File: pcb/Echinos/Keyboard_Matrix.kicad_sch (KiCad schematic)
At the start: 62 parts, among them J5 Joystick

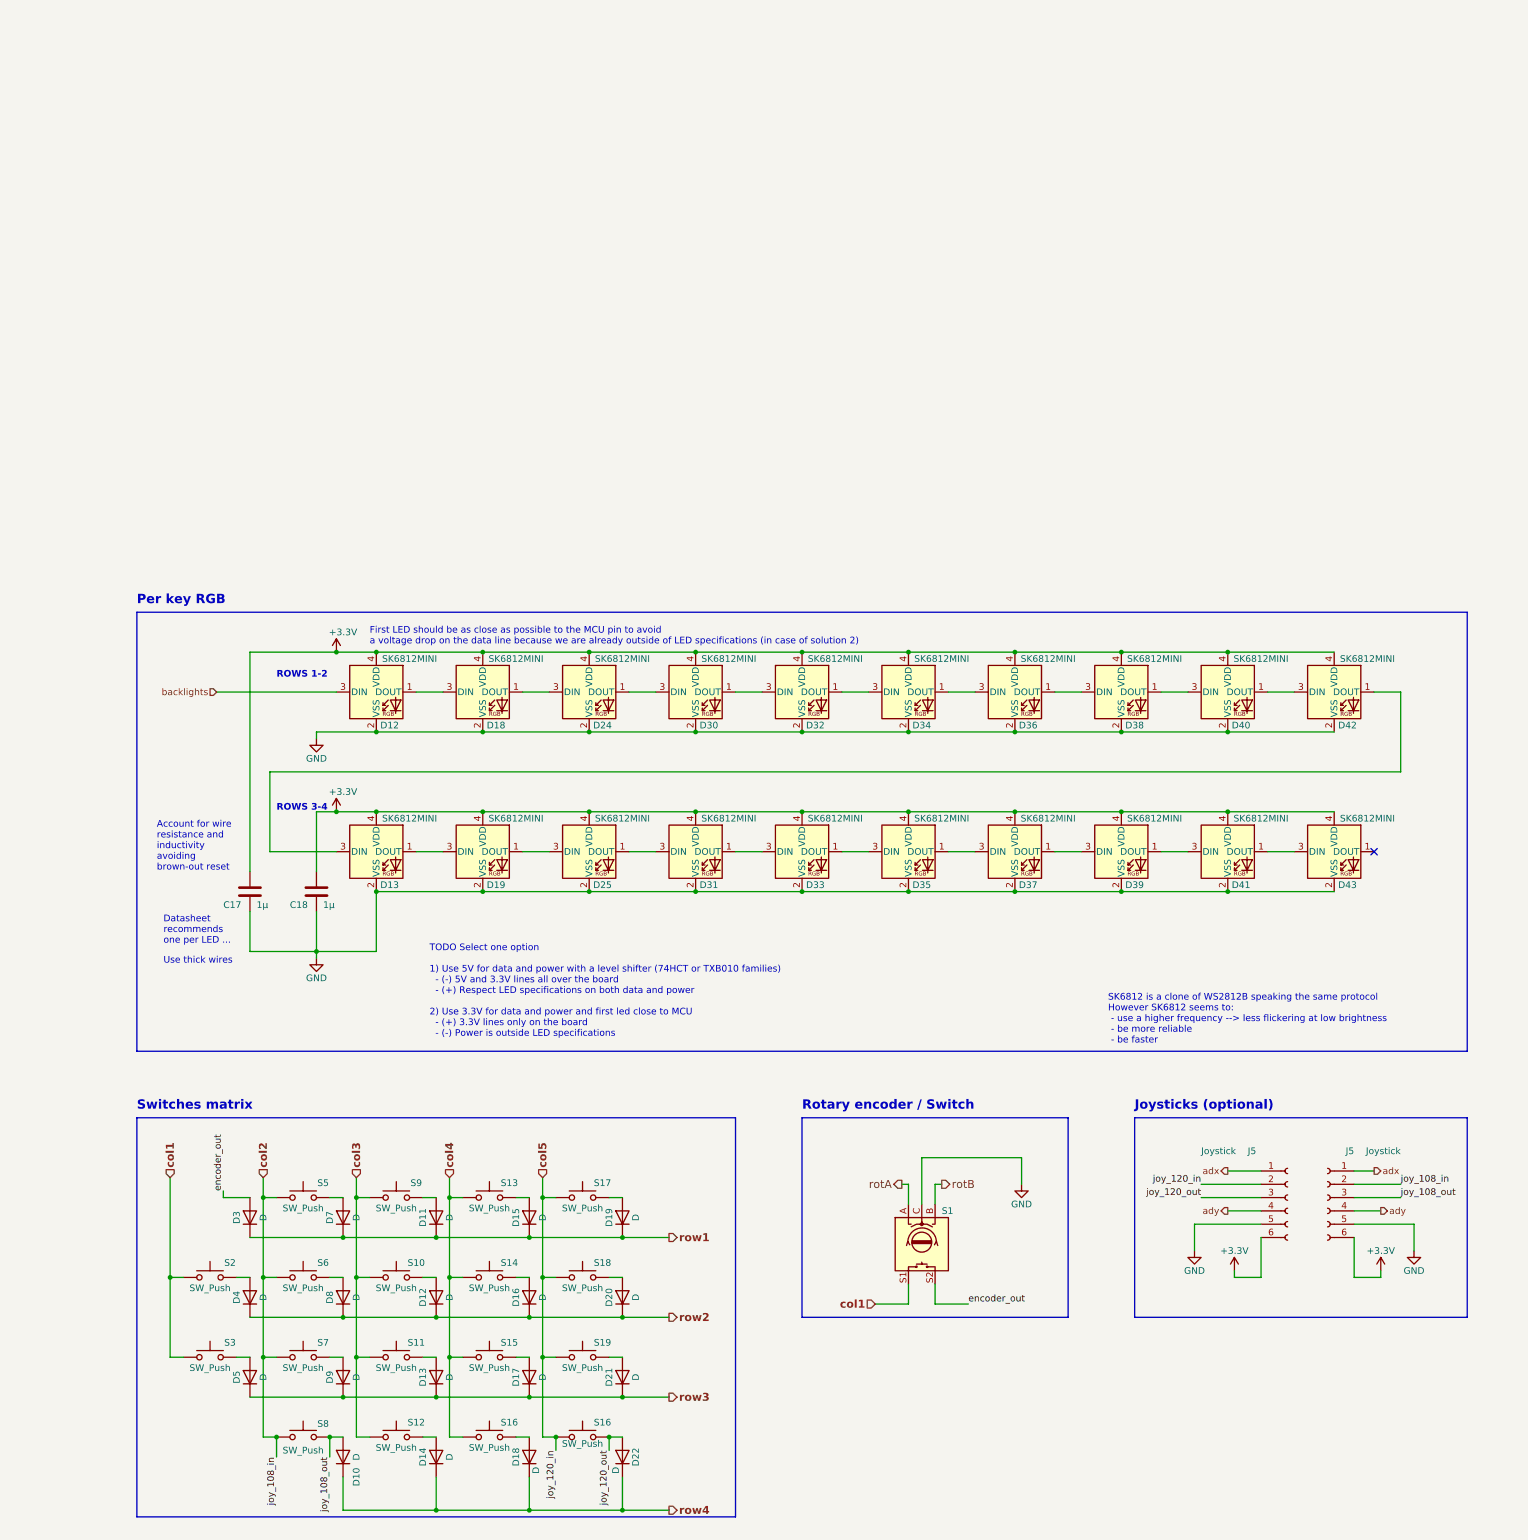
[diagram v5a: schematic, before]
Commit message: 🚧 [PCB] - Backup of a specific layout around MCU. Modules moved to a specific schematic page.
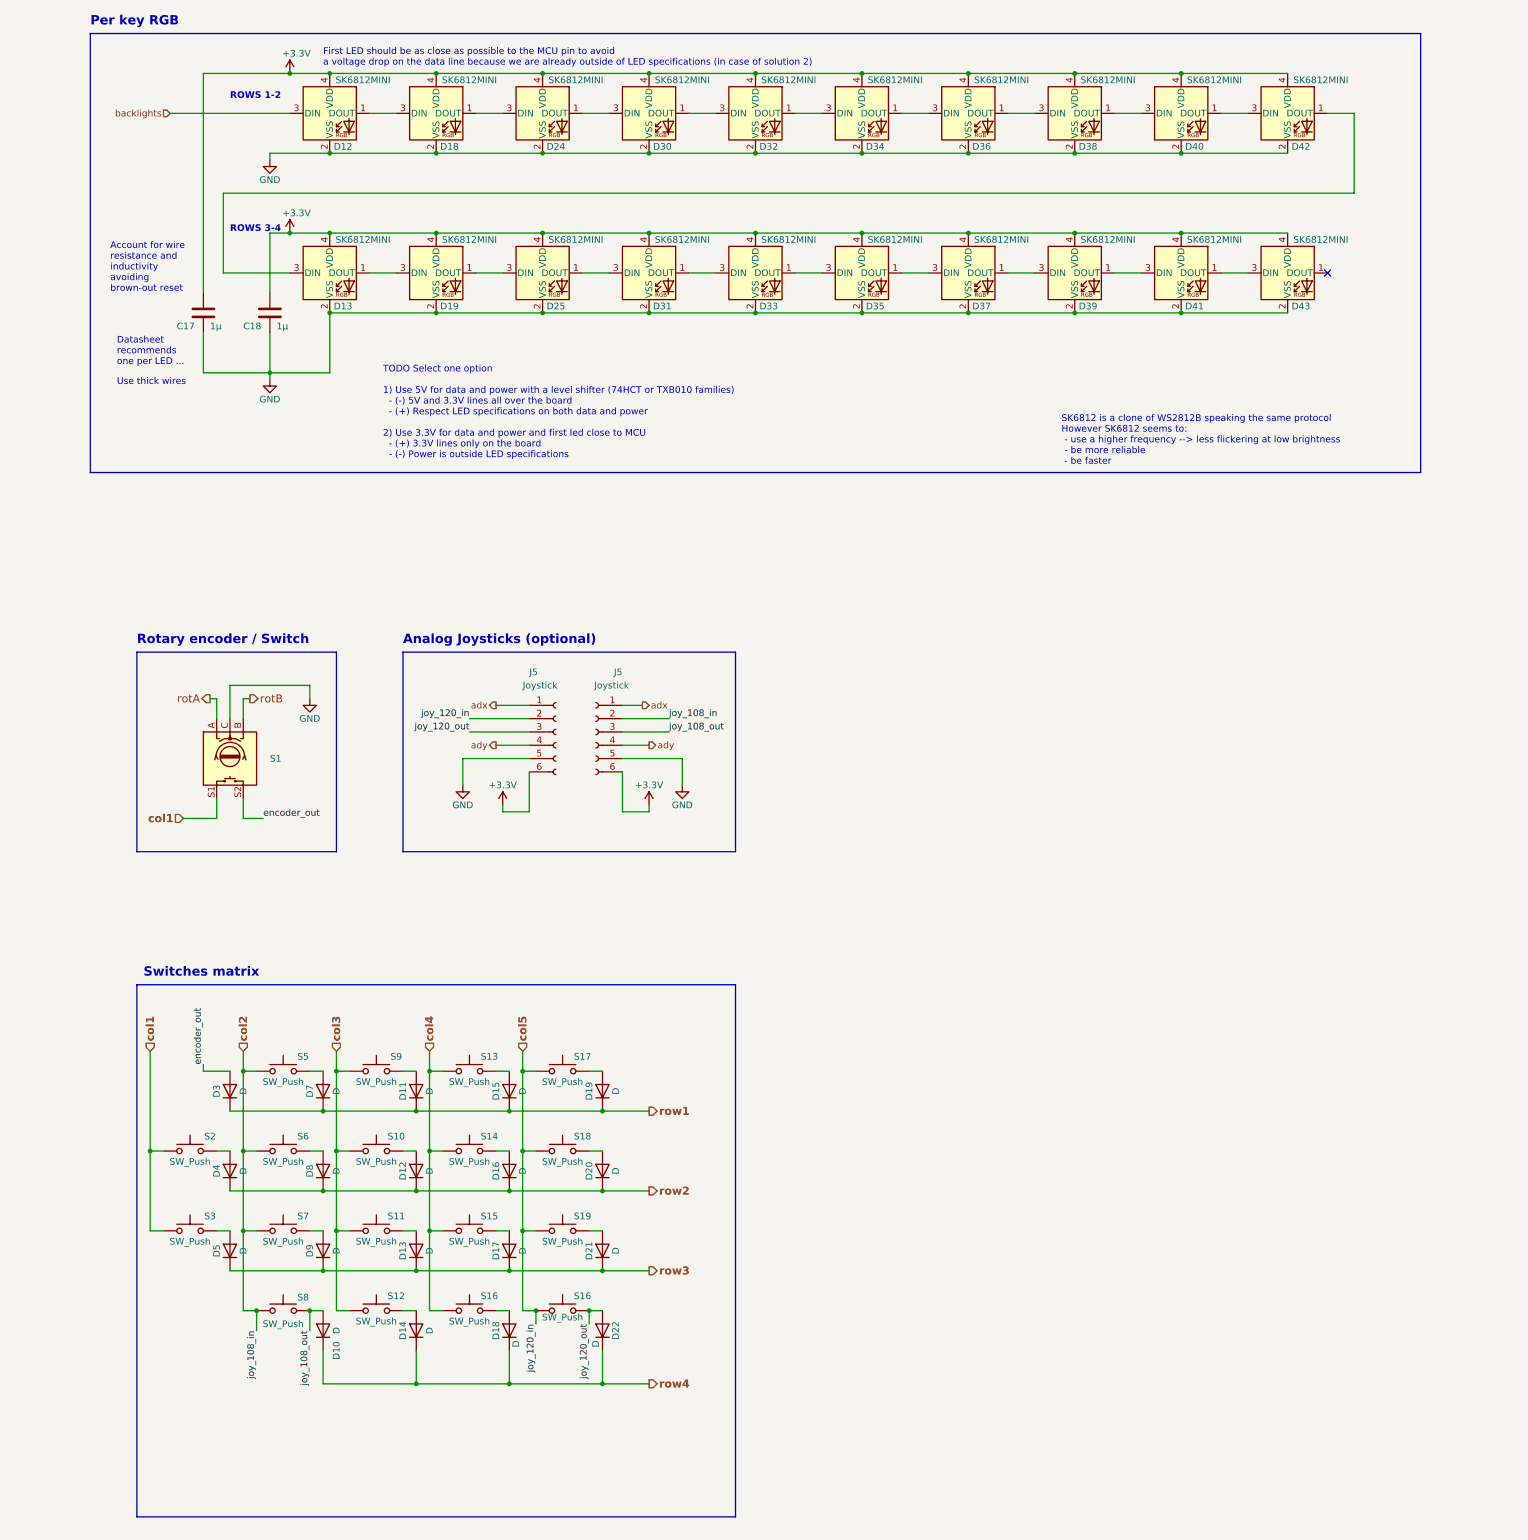
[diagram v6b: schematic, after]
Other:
- note added: "Analog Joysticks (optional)"
- note removed: "Joysticks (optional)"
- moved on the sheet: C17, C18, D10, D11, D12, D13, D14, D15, D16, D17, D18, D19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
